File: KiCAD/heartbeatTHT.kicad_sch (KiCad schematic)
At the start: 14 parts, among them Q1 BC547, Q2 BC547, Q3 BC557

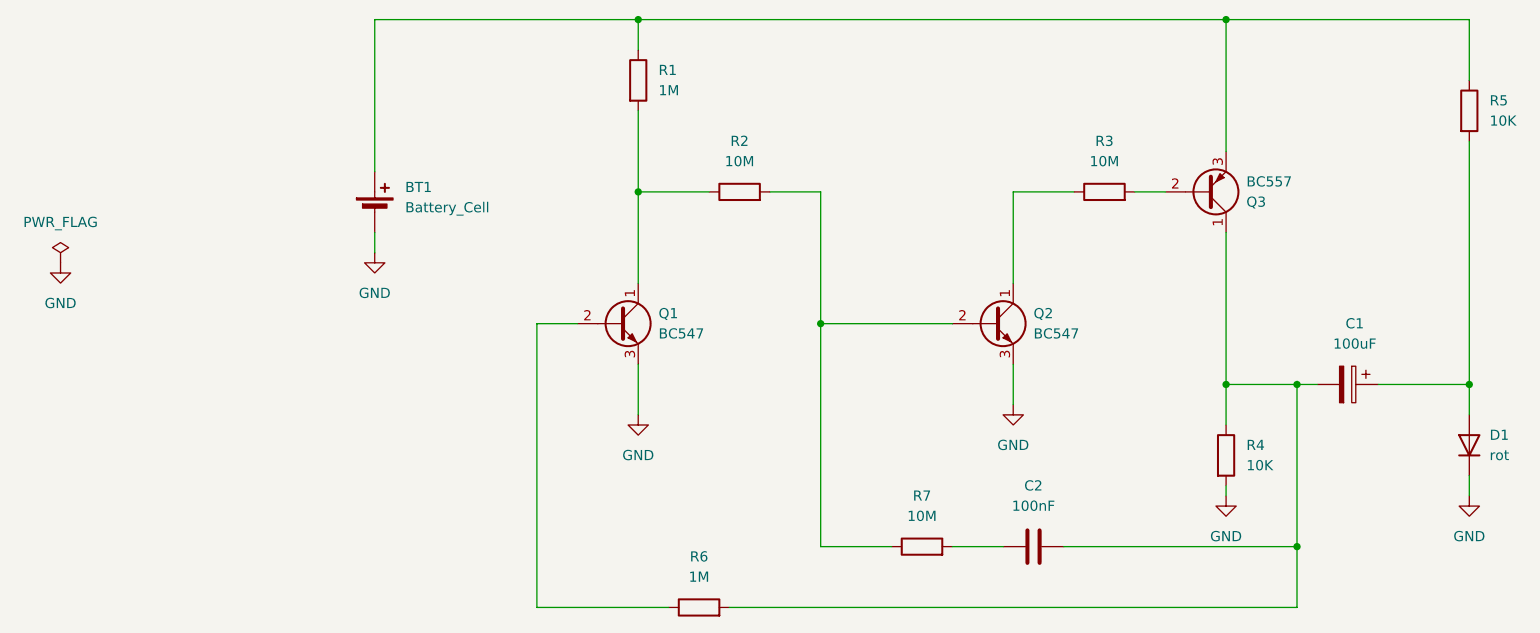
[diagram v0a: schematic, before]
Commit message: fixed minor issues, added logo, added simulation
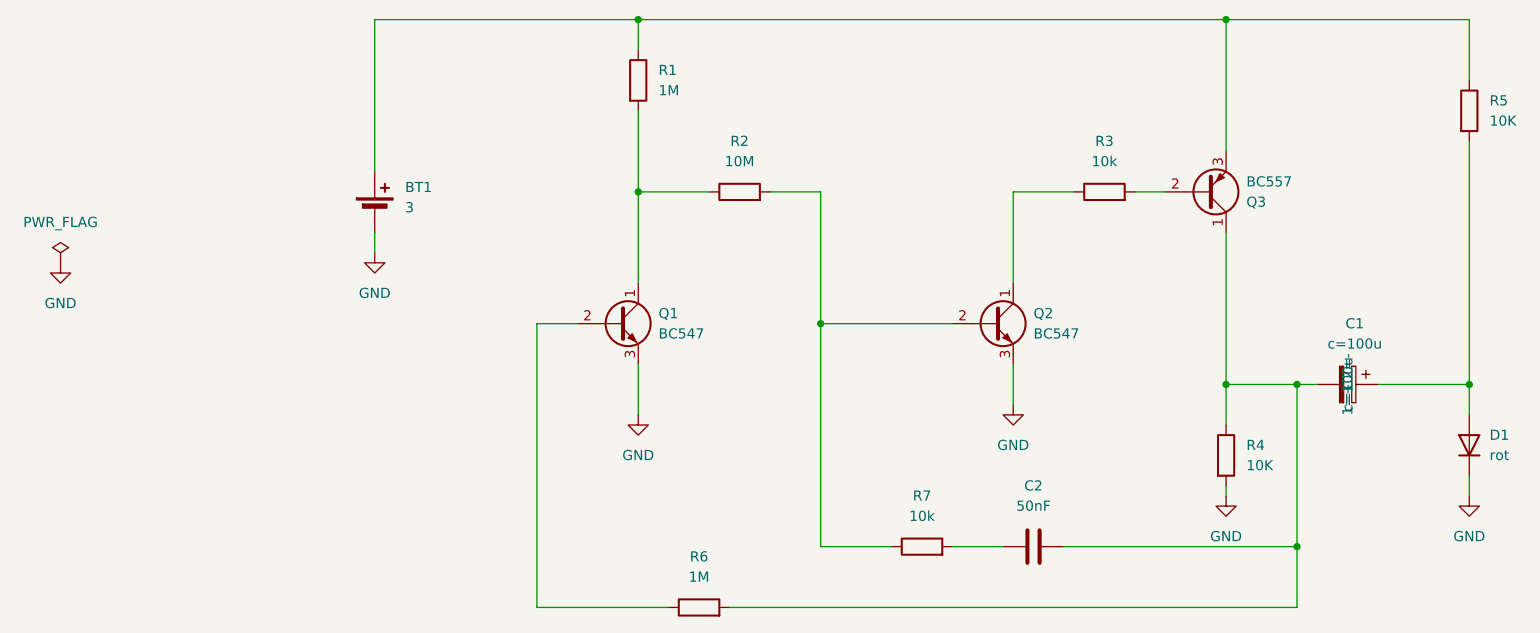
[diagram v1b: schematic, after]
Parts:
- BT1: value Battery_Cell -> 3
- C1: value 100uF -> ${SIM.PARAMS}
- C2: value 100nF -> 50nF
- R3, R7: value 10M -> 10k

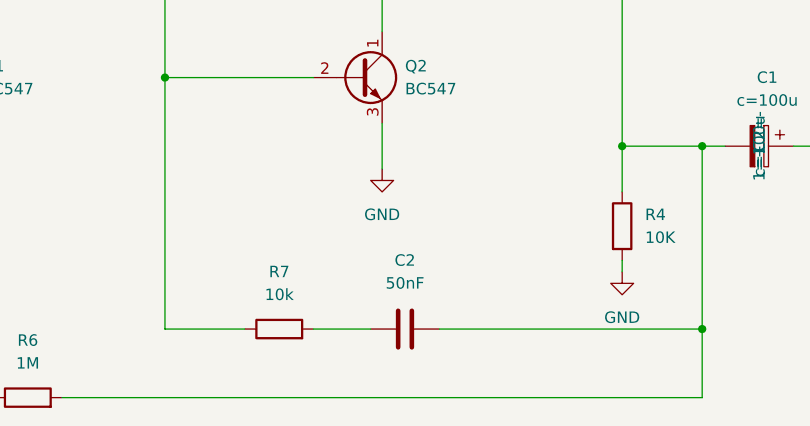
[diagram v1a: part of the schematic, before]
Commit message: changed 50uF to 100uF
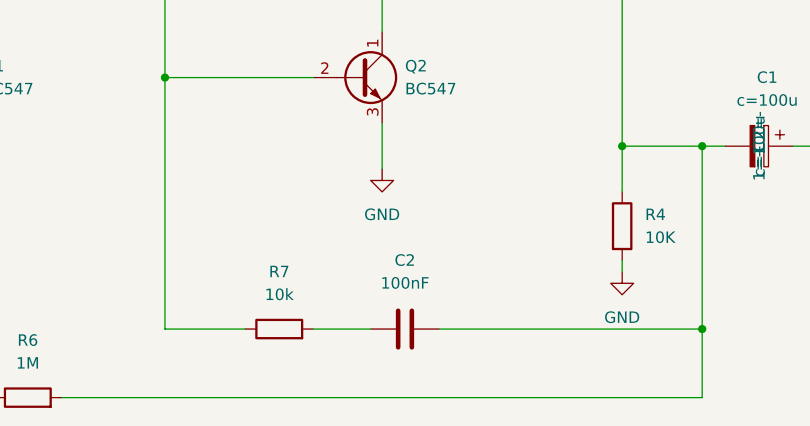
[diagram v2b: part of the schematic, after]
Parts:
- C2: value 50nF -> 100nF
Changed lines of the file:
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@@
 			)
 		)
-		(property "Value" "50nF"
+		(property "Value" "100nF"
 			(at 158.75 106.68 90)
 			(effects
